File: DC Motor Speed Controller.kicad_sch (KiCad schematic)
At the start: 0 parts

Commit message: Added all the components to Schematic Editor
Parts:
- added C1, C2: C, symbol Device:C
- added D1, D2, D3: 1N4007, Diode_THT:D_DO-41_SOD81_P10.16mm_Horizontal, symbol Diode:1N4007
- added J1, J2: Screw_Terminal_01x02, symbol Connector:Screw_Terminal_01x02
- added R1, R2: R, symbol Device:R
- added RV1: R_Potentiometer, symbol Device:R_Potentiometer
- added U1: NE555P, Package_DIP:DIP-8_W7.62mm, symbol Timer:NE555P
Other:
- title: (none) -> DC Motor Speed Controller

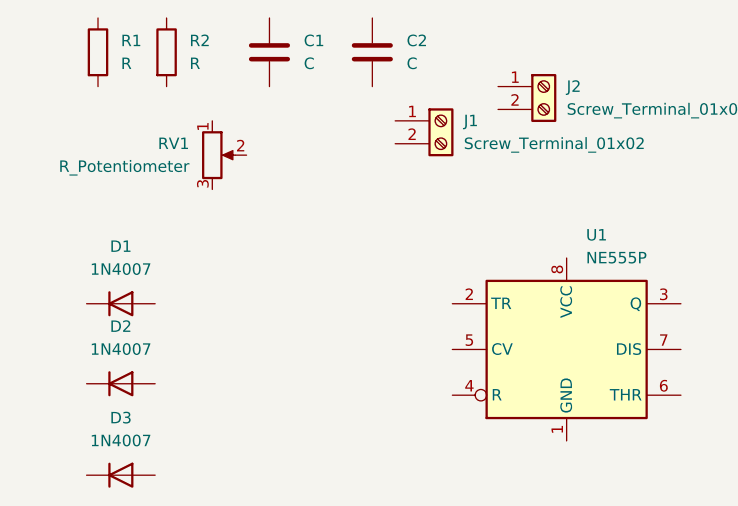
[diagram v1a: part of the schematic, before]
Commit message: Added the Transistor_BJT component
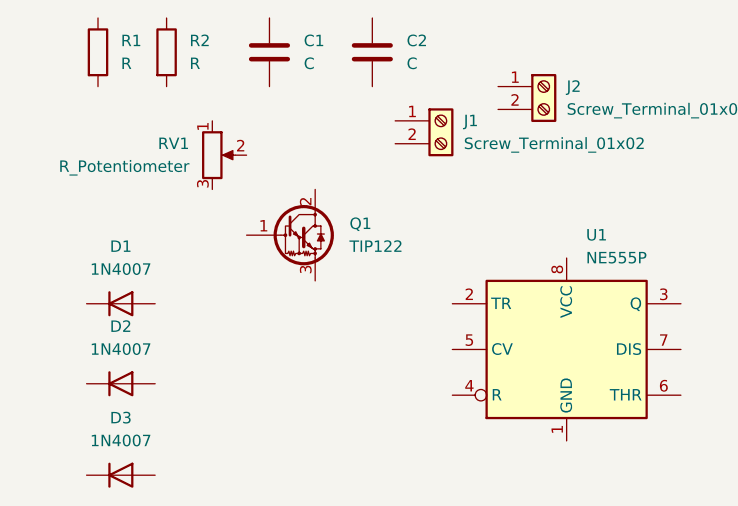
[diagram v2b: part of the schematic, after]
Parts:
- added Q1: TIP122, Package_TO_SOT_THT:TO-220-3_Vertical, symbol Transistor_BJT:TIP122
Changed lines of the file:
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@@
+	)
+	(symbol
+		(lib_id "Transistor_BJT:TIP122")
+		(at 40.64 39.37 0)
+		(unit 1)
+		(exclude_from_sim no)
+		(in_bom yes)
+		(on_board yes)
+		(dnp no)
+		(fields_autoplaced yes)
+		(property "Reference" "Q1"
+			(at 46.99 38.0999 0)
+			(effects
+				(font
+					(size 1.27 1.27)
+				)
+				(justify left)
+			)
+		)
+		(property "Value" "TIP122"
+			(at 46.99 40.6399 0)
+			(effects
+				(font
+					(size 1.27 1.27)
+				)
+				(justify left)
+			)
+		)
+		(property "Footprint" "Package_TO_SOT_THT:TO-220-3_Vertical"
+			(at 45.72 41.275 0)
+			(effects
+				(font
+					(size 1.27 1.27)
+					(italic yes)
+				)
+				(justify left)
+				(hide yes)
+			)
+		)
+		(property "Datasheet" "https://www.onsemi.com/pub/Collateral/TIP120-D.PDF"
+			(at 40.64 39.37 0)
+			(effects
+				(font
+					(size 1.27 1.27)
+				)
+				(justify left)
+				(hide yes)
+			)
+		)
+		(property "Description" "5A Ic, 100V Vce, Silicon Darlington Power NPN Transistor, TO-220"
+			(at 40.64 39.37 0)
+			(effects
+				(font
+					(size 1.27 1.27)
+				)
+				(hide yes)
+			)
+		)
+		(pin "1"
+		)
+		(pin "3"
+		)
+		(pin "2"
+		)
+		(instances
+			(project ""
+				(path "/f6006c76-6b8e-4b9c-acef-dbdcf88c8838"
+					(reference "Q1")
+					(unit 1)
+				)
+			)
+		)
 	)
 	(symbol

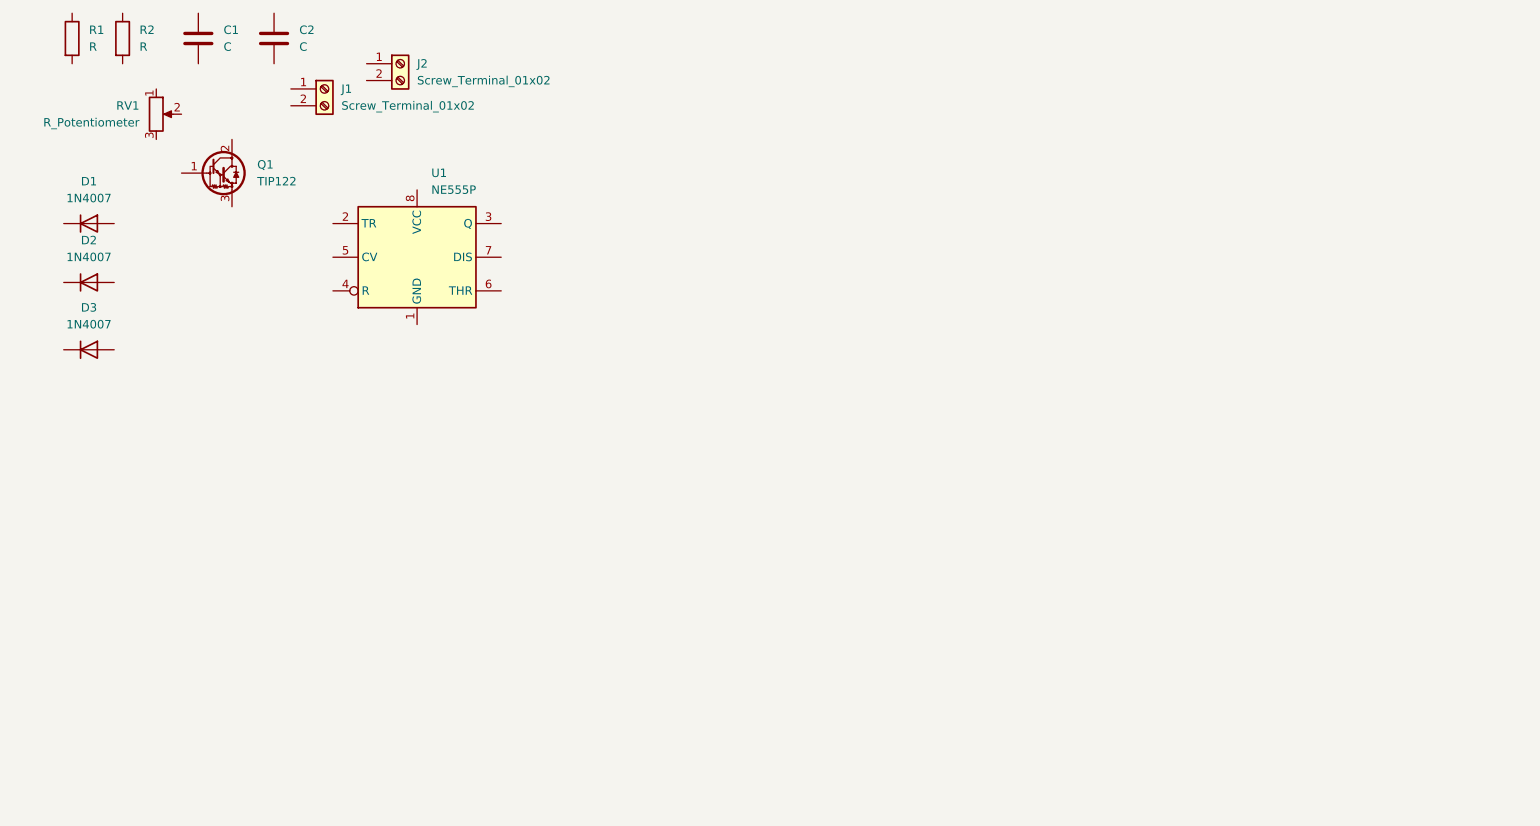
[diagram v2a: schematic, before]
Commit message: Moved components to place
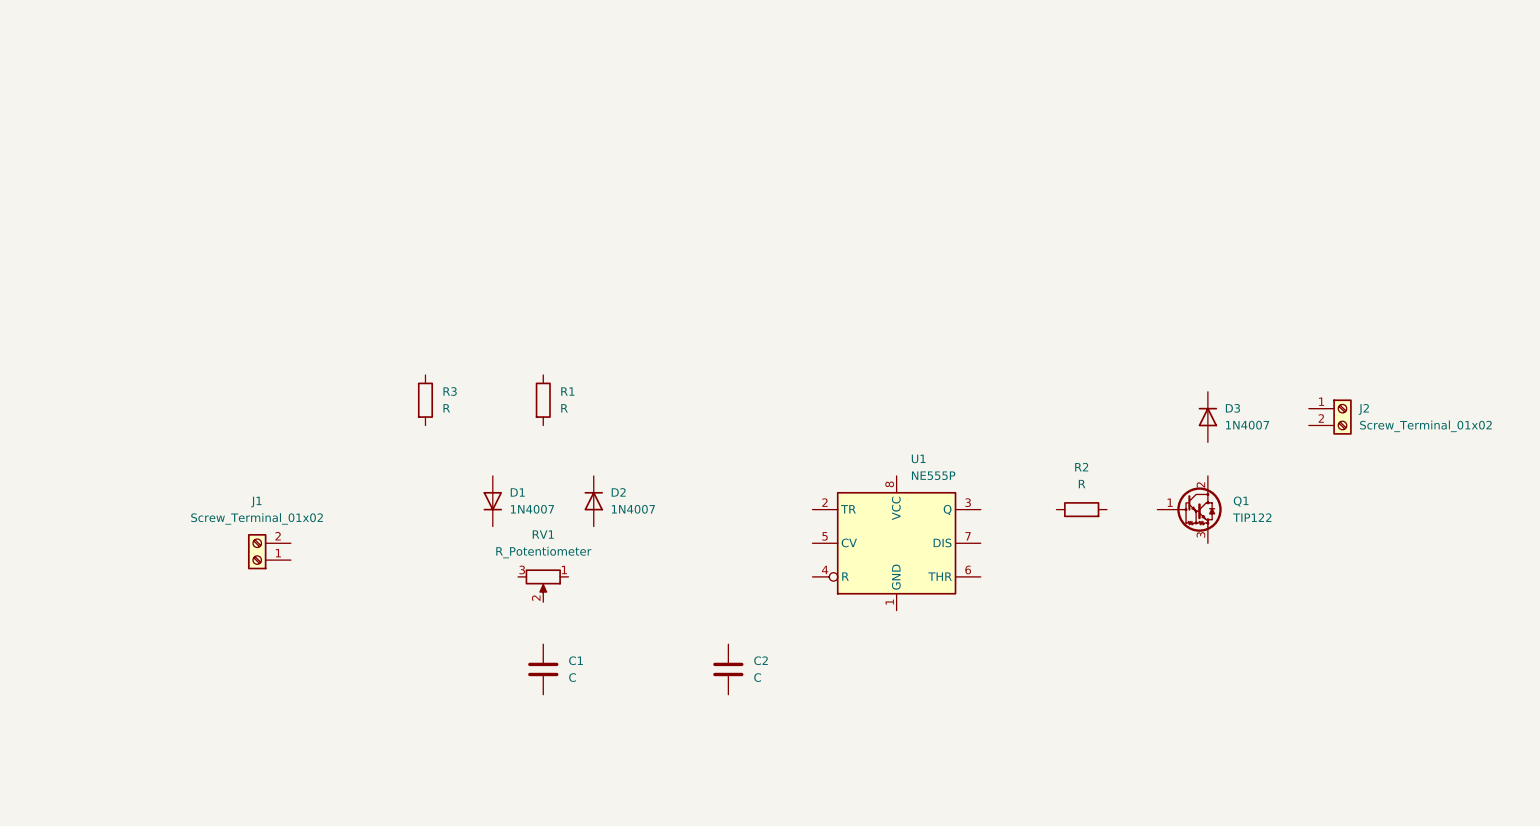
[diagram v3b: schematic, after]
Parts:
- added R3: R, symbol Device:R
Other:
- moved on the sheet: C1, C2, D1, D2, D3, J1, J2, Q1, R1, R2, RV1, U1

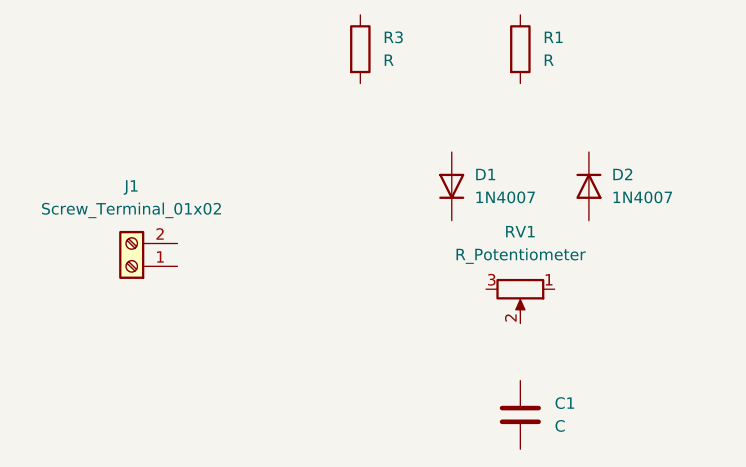
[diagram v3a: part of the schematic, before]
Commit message: Moved All the Components to Place
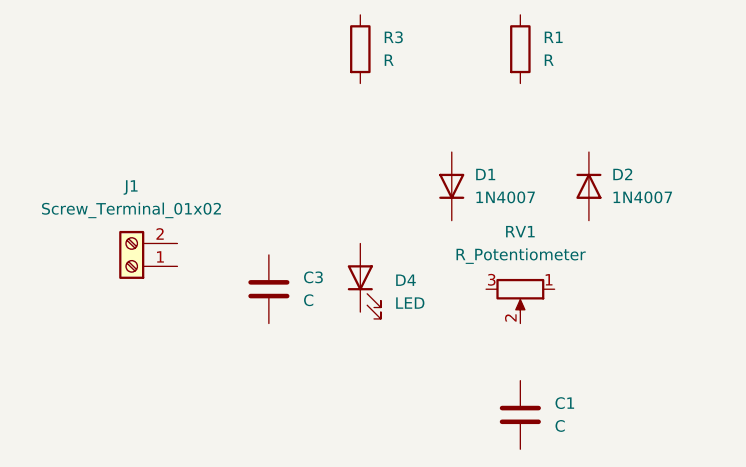
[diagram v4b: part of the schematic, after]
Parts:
- added C3: C, symbol Device:C
- added D4: LED, symbol Device:LED
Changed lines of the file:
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@@
+	)
+	(symbol
+		(lib_id "Device:LED")
+		(at 72.39 99.06 90)
+		(unit 1)
+		(exclude_from_sim no)
+		(in_bom yes)
+		(on_board yes)
+		(dnp no)
+		(fields_autoplaced yes)
+		(property "Reference" "D4"
+			(at 76.2 99.3774 90)
+			(effects
+				(font
+					(size 1.27 1.27)
+				)
+				(justify right)
+			)
+		)
+		(property "Value" "LED"
+			(at 76.2 101.9174 90)
+			(effects
+				(font
+					(size 1.27 1.27)
+				)
+				(justify right)
+			)
+		)
+		(property "Footprint" ""
+			(at 72.39 99.06 0)
+			(effects
+				(font
+					(size 1.27 1.27)
+				)
+				(hide yes)
+			)
+		)
+		(property "Datasheet" "~"
+			(at 72.39 99.06 0)
+			(effects
+				(font
+					(size 1.27 1.27)
+				)
+				(hide yes)
+			)
+		)
+		(property "Description" "Light emitting diode"
+			(at 72.39 99.06 0)
+			(effects
+				(font
+					(size 1.27 1.27)
+				)
+				(hide yes)
+			)
+		)
+		(property "Sim.Pins" "1=K 2=A"
+			(at 72.39 99.06 0)
+			(effects
+				(font
+					(size 1.27 1.27)
+				)
+				(hide yes)
+			)
+		)
+		(pin "1"
+		)
+		(pin "2"
+		)
+		(instances
+			(project ""
+				(path "/f6006c76-6b8e-4b9c-acef-dbdcf88c8838"
+					(reference "D4")
+					(unit 1)
+				)
+			)
+		)
+	)
+	(symbol
+		(lib_id "Device:C")
+		(at 62.23 100.33 0)
+		(unit 1)
+		(exclude_from_sim no)
+		(in_bom yes)
+		(on_board yes)
+		(dnp no)
+		(fields_autoplaced yes)
+		(property "Reference" "C3"
+			(at 66.04 99.0599 0)
+			(effects
+				(font
+					(size 1.27 1.27)
+				)
+				(justify left)
+			)
+		)
+		(property "Value" "C"
+			(at 66.04 101.5999 0)
+			(effects
+				(font
+					(size 1.27 1.27)
+				)
+				(justify left)
+			)
+		)
+		(property "Footprint" ""
+			(at 63.1952 104.14 0)
+			(effects
+				(font
+					(size 1.27 1.27)
+				)
+				(hide yes)
+			)
+		)
+		(property "Datasheet" "~"
+			(at 62.23 100.33 0)
+			(effects
+				(font
+					(size 1.27 1.27)
+				)
+				(hide yes)
+			)
+		)
+		(property "Description" "Unpolarized capacitor"
+			(at 62.23 100.33 0)
+			(effects
+				(font
+					(size 1.27 1.27)
+				)
+				(hide yes)
+			)
+		)
+		(pin "2"
+		)
+		(pin "1"
+		)
+		(instances
+			(project "DC Motor Speed Controller"
+				(path "/f6006c76-6b8e-4b9c-acef-dbdcf88c8838"
+					(reference "C3")
+					(unit 1)
+				)
+			)
+		)
 	)
 	(symbol

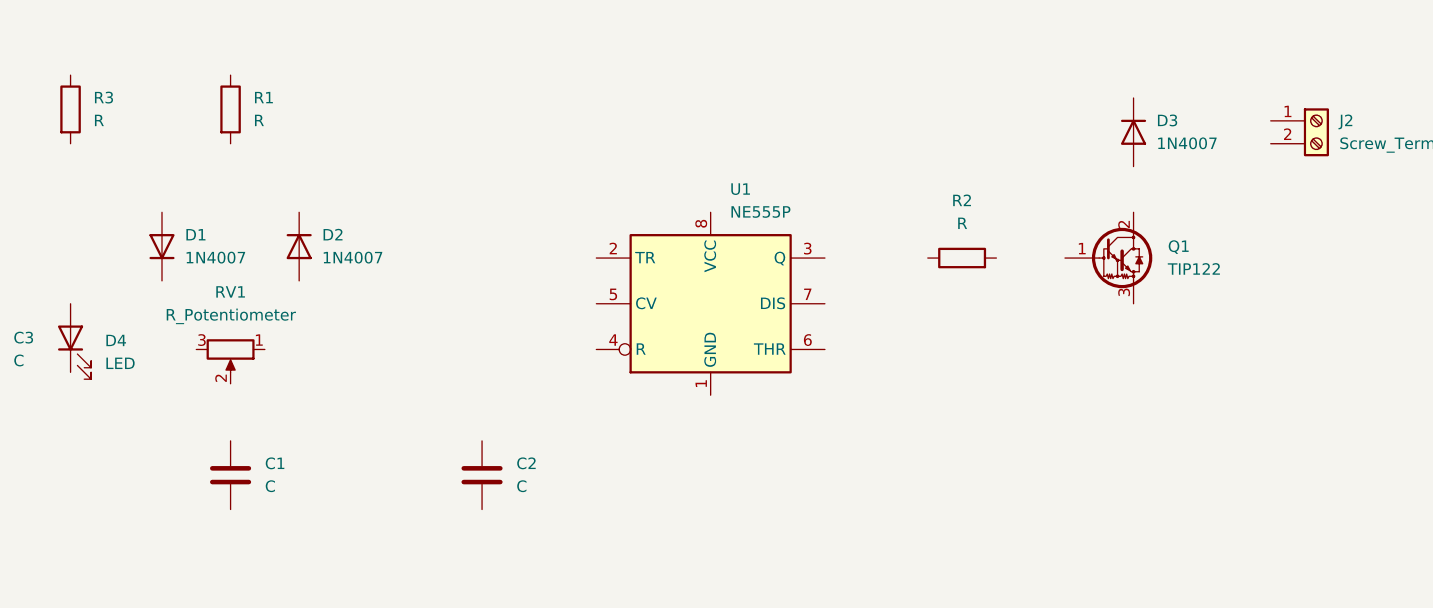
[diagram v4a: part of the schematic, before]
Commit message: Wired some Components
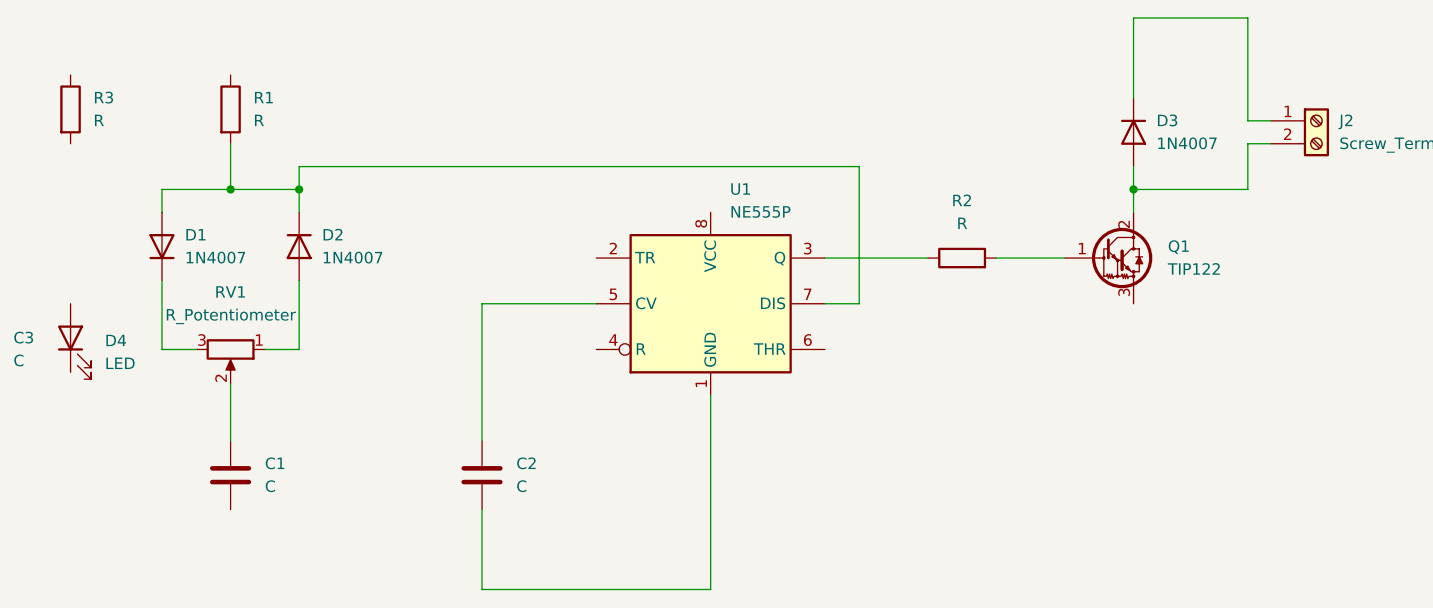
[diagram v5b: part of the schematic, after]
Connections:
- net at RV1.1: now also D2.2 (A)
- net at RV1.2: now also C1.1
- net at RV1.3: now also D1.1 (K)
- net at R2.1: now also U1.3 (Q)
- net at R2.2: now also Q1.1 (B)
- net at Q1.2 (C): now also D3.2 (A), J2.2 (Pin_2)
- net at C2.1: now also U1.5 (CV)
- net at C2.2: now also U1.1 (GND)
- net at D3.1 (K): now also J2.1 (Pin_1)
- net at U1.7 (DIS): now also D1.2 (A), D2.1 (K), R1.2

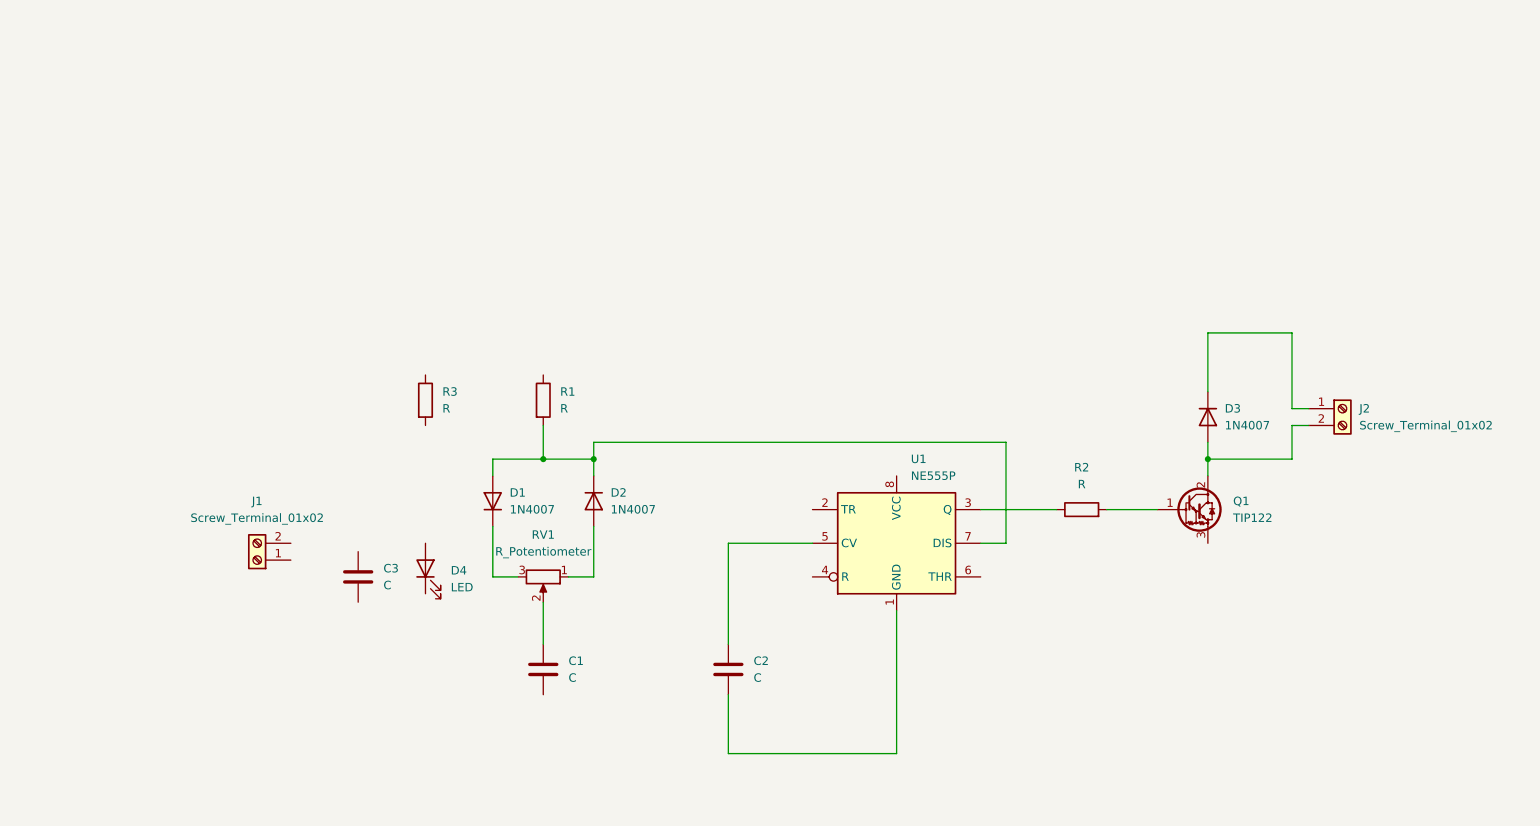
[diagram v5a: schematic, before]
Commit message: Connected all the components with Wires
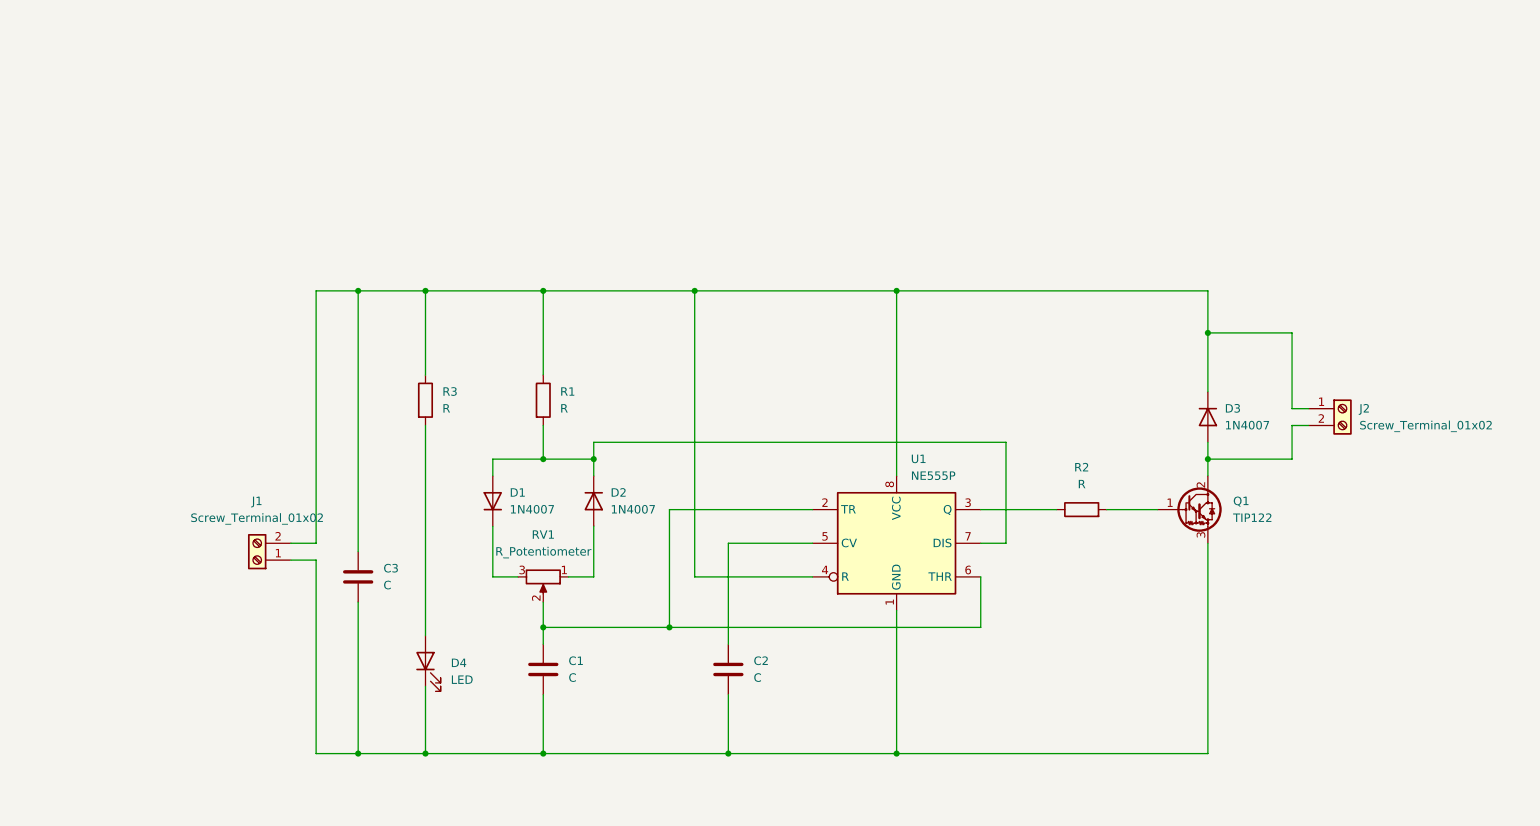
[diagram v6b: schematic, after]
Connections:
- net at C1.1, RV1.2: now also U1.2 (TR), U1.6 (THR)
- net at D4.1 (K): now also C1.2, C2.2, C3.2, J1.1 (Pin_1), Q1.3 (E), U1.1 (GND)
- net at D4.2 (A): now also R3.2
- net at C3.1: now also D3.1 (K), J1.2 (Pin_2), J2.1 (Pin_1), R1.1, R3.1, U1.4 (R), U1.8 (VCC)
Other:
- moved on the sheet: D4
